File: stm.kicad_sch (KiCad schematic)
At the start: 0 parts

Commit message: added some components
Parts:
- added C? (x4): 100n, symbol Device:C
- added C?: 10n, symbol Device:C
- added C? (x2): 1u, symbol Device:C
- added C?: 10u, symbol Device:C
- added FB?: FerriteBead, symbol Device:FerriteBead
- added U?: STM32F103C8Tx, Package_QFP:LQFP-48_7x7mm_P0.5mm, symbol MCU_ST_STM32F1:STM32F103C8Tx
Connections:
- new net: C?.1, FB?.2
- new net +3.3V: C?.1, C?.1, C?.1, C?.1, C?.1, C?.1, C?.1, FB?.1, U?.1 (VBAT), U?.24 (VDD), U?.36 (VDD), U?.48 (VDD), U?.9 (VDDA)
- new net GND: C?.2, C?.2, C?.2, C?.2, C?.2, C?.2, C?.2, C?.2, U?.23 (VSS), U?.35 (VSS), U?.47 (VSS), U?.8 (VSSA)

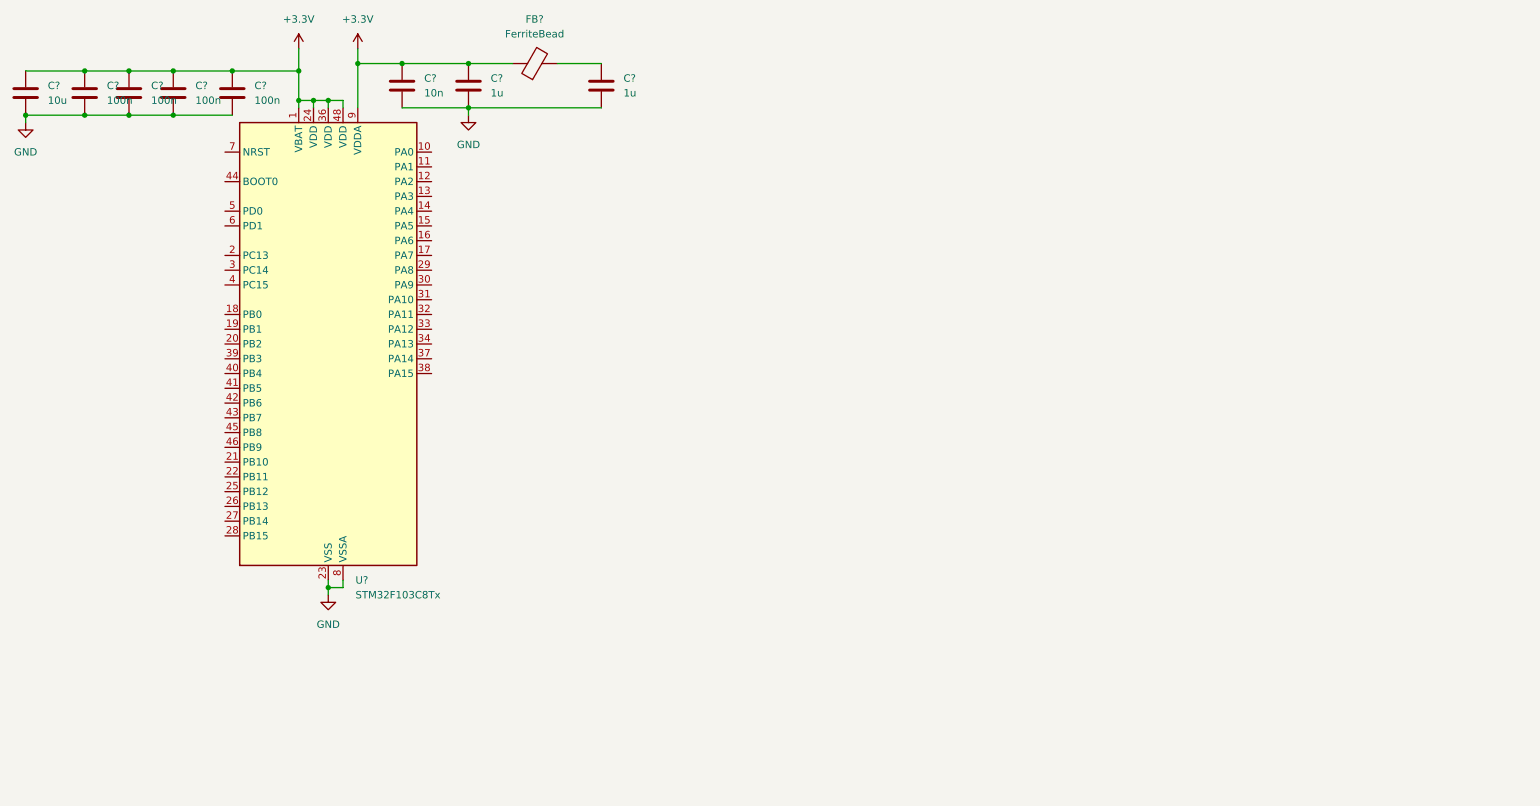
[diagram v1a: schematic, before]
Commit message: added more to schematic
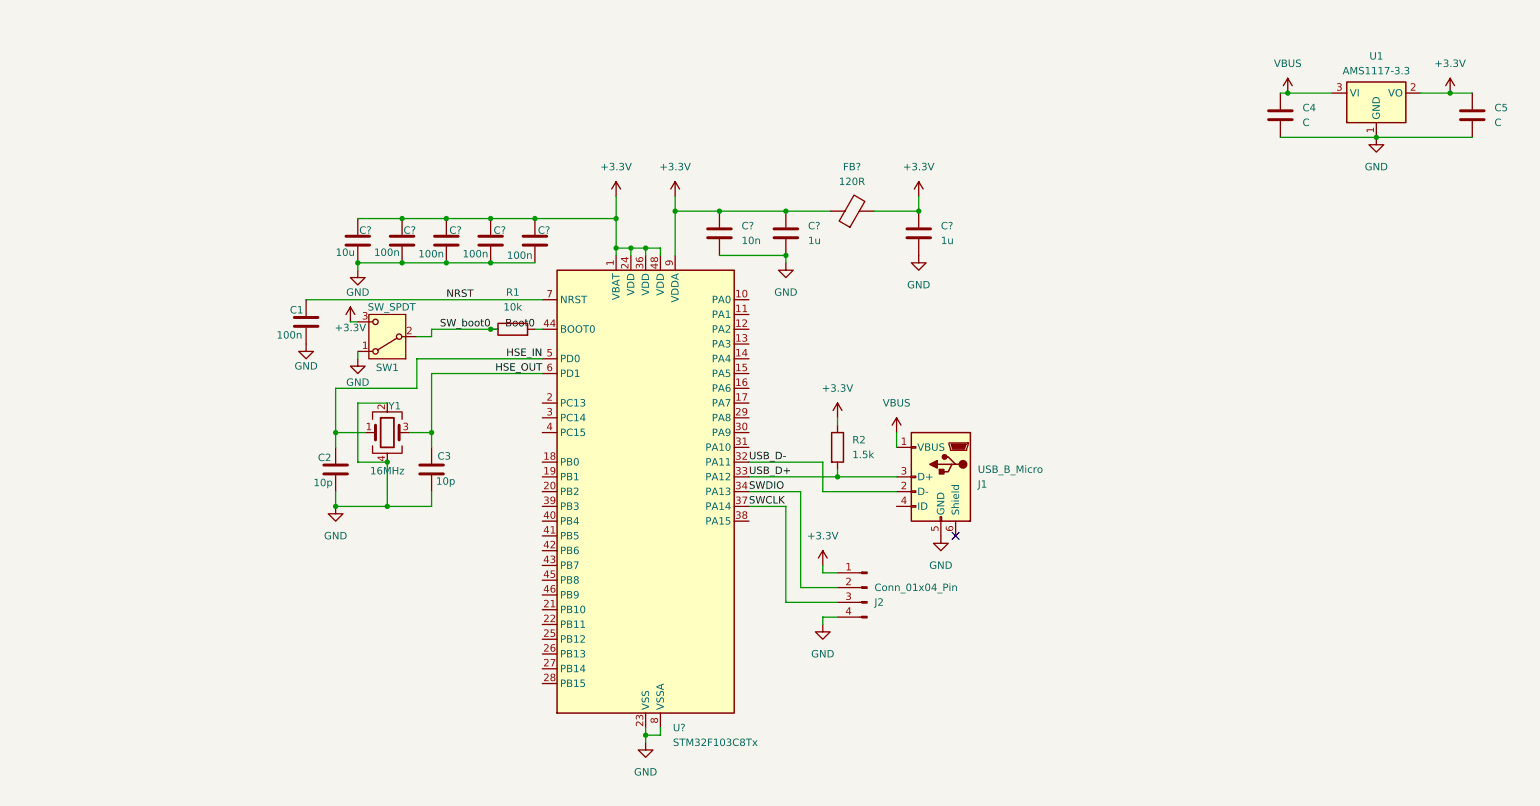
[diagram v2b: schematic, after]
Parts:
- added C1: 100n, symbol Device:C
- added C2, C3: 10p, symbol Device:C
- added C4, C5: C, symbol Device:C
- added J1: USB_B_Micro, symbol Connector:USB_B_Micro
- added J2: Conn_01x04_Pin, symbol Connector:Conn_01x04_Pin
- added R1: 10k, symbol Device:R
- added R2: 1.5k, symbol Device:R
- added SW1: SW_SPDT, symbol Switch:SW_SPDT
- added U1: AMS1117-3.3, Package_TO_SOT_SMD:SOT-223-3_TabPin2, symbol Regulator_Linear:AMS1117-3.3
- added Y1: 16MHz, symbol Device:Crystal_GND24
- FB?: value FerriteBead -> 120R
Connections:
- net +3.3V: now also C?.1, FB?.2, C5.1, J2.1 (Pin_1), R2.1, SW1.3 (C), U1.2 (VO)
- net GND: now also C1.1, C2.2, C3.2, C4.2, C5.2, J1.5 (GND), J2.4 (Pin_4), SW1.1 (A), U1.1 (GND), Y1.2, Y1.4
- net USB_D-: now reaches U?.32 (PA11)
- net USB_D-: now also J1.2 (D-)
- net USB_D+: now reaches U?.33 (PA12)
- net USB_D+: now also J1.3 (D+), R2.2
- net SWDIO: now reaches U?.34 (PA13)
- net SWDIO: now also J2.2 (Pin_2)
- net SWCLK: now reaches U?.37 (PA14)
- net SWCLK: now also J2.3 (Pin_3)
- net Boot0: now reaches U?.44 (BOOT0)
- net Boot0: now also R1.2
- net HSE_IN: now reaches U?.5 (PD0)
- net HSE_IN: now also C2.1, Y1.1
- net HSE_OUT: now reaches U?.6 (PD1)
- net HSE_OUT: now also C3.1, Y1.3
- net NRST: now reaches U?.7 (NRST)
- net NRST: now also C1.2
- new net SW_boot0: R1.1, SW1.2 (B)
- new net VBUS: C4.1, J1.1 (VBUS), U1.3 (VI)
- no-connect marks 0 -> 1
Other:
- moved on the sheet: C?, FB?, U?

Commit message: done with schematic
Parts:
- added D1: LED, LED_SMD:LED_0805_2012Metric_Pad1.15x1.40mm_HandSolder, symbol Device:LED
- added J3, J4: Conn_01x04_Pin, Connector_PinHeader_2.54mm:PinHeader_1x04_P2.54mm_Vertical, symbol Connector:Conn_01x04_Pin
- added R3, R4, R5: 1.5k, Resistor_SMD:R_0402_1005Metric_Pad0.72x0.64mm_HandSolder, symbol Device:R
- C1, C2, C3: footprint (none) -> Capacitor_SMD:C_0805_2012Metric_Pad1.18x1.45mm_HandSolder
- C10, C11, C12, C13, C6, C7, C8, C9: renamed from C?; footprint (none) -> Capacitor_SMD:C_0805_2012Metric_Pad1.18x1.45mm_HandSolder
- C4, C5: value C -> 22u; footprint (none) -> Capacitor_SMD:C_0805_2012Metric_Pad1.18x1.45mm_HandSolder
- FB1: renamed from FB?; footprint (none) -> Inductor_SMD:L_0603_1608Metric_Pad1.05x0.95mm_HandSolder
- J1: footprint (none) -> Connector_USB:USB_Micro-B_Molex_47346-0001
- J2: footprint (none) -> Connector_PinHeader_2.54mm:PinHeader_1x04_P2.54mm_Vertical
- R1, R2: footprint (none) -> Resistor_SMD:R_0402_1005Metric_Pad0.72x0.64mm_HandSolder
- SW1: footprint (none) -> Button_Switch_SMD:SW_SPST_B3S-1100
- Y1: footprint (none) -> Crystal:Crystal_SMD_3225-4Pin_3.2x2.5mm_HandSoldering
- gave numbers to parts that had none: 1
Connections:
- net +3.3V: now also D1.2 (A), J3.1 (Pin_1), J4.1 (Pin_1), R4.1, R5.1
- net GND: now also J3.4 (Pin_4), J4.4 (Pin_4), R3.2
- net I2C2_SCL: now reaches U2.21 (PB10)
- net I2C2_SCL: now also J4.2 (Pin_2), R4.2
- net I2C2_SDA: now reaches U2.22 (PB11)
- net I2C2_SDA: now also J4.3 (Pin_3), R5.2
- net UART_TX: now reaches U2.42 (PB6)
- net UART_TX: now also J3.2 (Pin_2)
- net UART_RX: now reaches U2.43 (PB7)
- net UART_RX: now also J3.3 (Pin_3)
- new net PWR_LED_Cathode: D1.1 (K), R3.1
- no-connect marks 1 -> 28
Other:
- note added: "1x 100nF cap per VDD or VBAT pin"
- note added: "Microcontroller and Micro USB"
- note added: "Pin-out done using STM32CubeIDE software"
- note added: "Power Supply"
- note added: "VBUS from USB con (typ +5V). 22u min in/out cap."
- note added: "application note AN4879 - 2.1: USB implementation on STM32 products"
- note added: "extra filtering for VDDA"
- company: (none) -> I love KiCAD inc.
- title: (none) -> STM32 Microcontroller
- moved on the sheet: C4, C5, U1

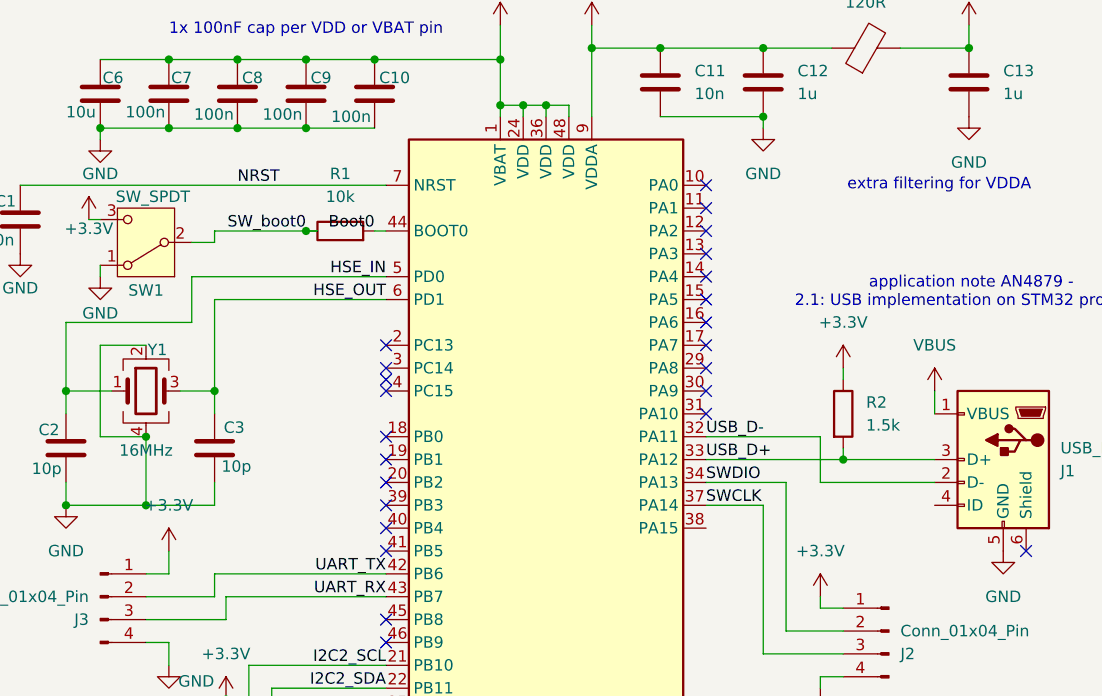
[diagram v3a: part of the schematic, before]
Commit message: fixed all DRC errors
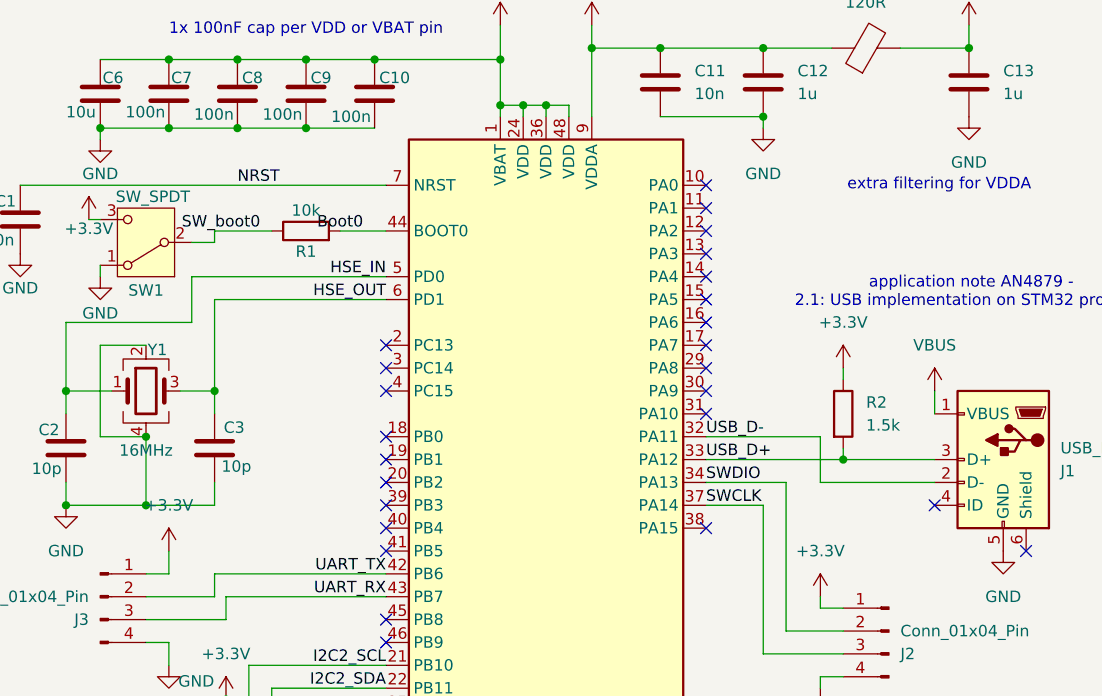
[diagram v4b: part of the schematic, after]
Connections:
- no-connect marks 28 -> 29
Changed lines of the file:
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@@
 	)
 	(junction
-		(at 105.41 69.85)
-		(diameter 0)
-		(color 0 0 0 0)
-	)
-	(junction
 		(at 165.1 95.25)
 		(diameter 0)
@@
 	)
 	(no_connect
-		(at 114.3 130.81)
+		(at 149.86 102.87)
 	)
 	(no_connect
-		(at 114.3 86.36)
+		(at 114.3 130.81)
 	)
 	(no_connect
@@
 	)
 	(no_connect
-		(at 114.3 87.63)
-	)
-	(no_connect
 		(at 114.3 102.87)
 	)
@@
 	)
 	(no_connect
+		(at 175.26 100.33)
+	)
+	(no_connect
+		(at 114.3 87.63)
+	)
+	(no_connect
 		(at 149.86 85.09)
 	)
@@
 	(wire
 		(pts
-			(xy 105.41 58.42) (xy 113.03 58.42)
+			(xy 95.25 69.85) (xy 101.6 69.85)
 		)
 		(stroke
@@
 	(wire
 		(pts
-			(xy 134.62 139.7) (xy 132.08 139.7)
+			(xy 105.41 58.42) (xy 113.03 58.42)
 		)
 		(stroke
@@
 	(wire
 		(pts
-			(xy 78.74 87.63) (xy 83.82 87.63)
+			(xy 134.62 139.7) (xy 132.08 139.7)
 		)
 		(stroke
@@
 	(wire
 		(pts
-			(xy 87.63 113.03) (xy 96.52 113.03)
+			(xy 78.74 87.63) (xy 83.82 87.63)
 		)
 		(stroke
@@
 	(wire
 		(pts
-			(xy 223.52 29.21) (xy 231.14 29.21)
+			(xy 87.63 113.03) (xy 96.52 113.03)
 		)
 		(stroke
@@
 	(wire
 		(pts
-			(xy 95.25 97.79) (xy 95.25 100.33)
+			(xy 223.52 29.21) (xy 231.14 29.21)
 		)
 		(stroke
@@
 	(wire
 		(pts
-			(xy 156.21 100.33) (xy 149.86 100.33)
+			(xy 95.25 97.79) (xy 95.25 100.33)
 		)
 		(stroke
@@
 	(wire
 		(pts
-			(xy 95.25 87.63) (xy 95.25 77.47)
+			(xy 156.21 100.33) (xy 149.86 100.33)
 		)
 		(stroke
@@
 	(wire
 		(pts
-			(xy 106.68 69.85) (xy 105.41 69.85)
+			(xy 95.25 87.63) (xy 95.25 77.47)
 		)
 		(stroke
@@
 	(wire
 		(pts
-			(xy 95.25 69.85) (xy 105.41 69.85)
-		)
-		(stroke
-			(width 0)
-			(type default)
-		)
-	)
-	(wire
-		(pts
 			(xy 162.56 97.79) (xy 162.56 92.71)
 		)
@@
 	(wire
 		(pts
-			(xy 113.03 69.85) (xy 114.3 69.85)
-		)
-		(stroke
-			(width 0)
-			(type default)
-		)
-	)
-	(wire
-		(pts
 			(xy 92.71 71.12) (xy 95.25 71.12)
 		)
@@
 	(wire
 		(pts
+			(xy 109.22 69.85) (xy 114.3 69.85)
+		)
+		(stroke
+			(width 0)
+			(type default)
+		)
+	)
+	(wire
+		(pts
 			(xy 156.21 58.42) (xy 156.21 57.15)
 		)
@@
 	)
 	(label "Boot0"
-		(at 113.03 69.85 180)
+		(at 111.76 69.85 180)
 		(effects
 			(font
@@
 	)
 	(label "SW_boot0"
-		(at 105.41 69.85 180)
+		(at 100.33 69.85 180)
 		(effects
 			(font
@@
 	)
 	(symbol
-		(lib_id "power:GND")
-		(at 179.07 57.15 0)
+		(lib_id "Device:R")
+		(at 105.41 69.85 90)
 		(unit 1)
 		(exclude_from_sim no)
@@
 		(on_board yes)
 		(dnp no)
-		(fields_autoplaced yes)
-		(property "Reference" "#PWR06"
-			(at 179.07 63.5 0)
+		(property "Reference" "R1"
+			(at 105.41 72.136 90)
 			(effects
 				(font
 					(size 1.27 1.27)
 				)
-				(hide yes)
 			)
 		)
-		(property "Value" "GND"
-			(at 179.07 62.23 0)
+		(property "Value" "10k"
+			(at 105.41 67.564 90)
 			(effects
 				(font
@@
 			)
 		)
-		(property "Footprint" ""
-			(at 179.07 57.15 0)
+		(property "Footprint" "Resistor_SMD:R_0402_1005Metric_Pad0.72x0.64mm_HandSolder"
+			(at 105.41 71.628 90)
 			(effects
 				(font
@@
 			)
 		)
-		(property "Datasheet" ""
-			(at 179.07 57.15 0)
+		(property "Datasheet" "~"
+			(at 105.41 69.85 0)
 			(effects
 				(font
@@
 			)
 		)
-		(property "Description" "Power symbol creates a global label with name \"GND\" , ground"
-			(at 179.07 57.15 0)
+		(property "Description" "Resistor"
+			(at 105.41 69.85 0)
 			(effects
 				(font
@@
 			)
 		)
+		(pin "2"
+		)
 		(pin "1"
 		)
 		(instances
-			(project "stm"
+			(project ""
 				(path "/ec652fd4-c034-4510-acc4-5860b93bab77"
-					(reference "#PWR06")
+					(reference "R1")
 					(unit 1)
 				)
@@
 	)
 	(symbol
-		(lib_id "Device:R")
-		(at 109.22 69.85 90)
+		(lib_id "power:GND")
+		(at 179.07 57.15 0)
 		(unit 1)
 		(exclude_from_sim no)
@@
 		(dnp no)
 		(fields_autoplaced yes)
-		(property "Reference" "R1"
-			(at 109.22 63.5 90)
+		(property "Reference" "#PWR06"
+			(at 179.07 63.5 0)
 			(effects
 				(font
 					(size 1.27 1.27)
 				)
+				(hide yes)
 			)
 		)
-		(property "Value" "10k"
-			(at 109.22 66.04 90)
+		(property "Value" "GND"
+			(at 179.07 62.23 0)
 			(effects
 				(font
@@
 			)
 		)
-		(property "Footprint" "Resistor_SMD:R_0402_1005Metric_Pad0.72x0.64mm_HandSolder"
-			(at 109.22 71.628 90)
+		(property "Footprint" ""
+			(at 179.07 57.15 0)
 			(effects
 				(font
@@
 			)
 		)
-		(property "Datasheet" "~"
-			(at 109.22 69.85 0)
+		(property "Datasheet" ""
+			(at 179.07 57.15 0)
 			(effects
 				(font
@@
 			)
 		)
-		(property "Description" "Resistor"
-			(at 109.22 69.85 0)
+		(property "Description" "Power symbol creates a global label with name \"GND\" , ground"
+			(at 179.07 57.15 0)
 			(effects
 				(font
@@
 			)
 		)
-		(pin "2"
-		)
 		(pin "1"
 		)
 		(instances
-			(project ""
+			(project "stm"
 				(path "/ec652fd4-c034-4510-acc4-5860b93bab77"
-					(reference "R1")
+					(reference "#PWR06")
 					(unit 1)
 				)

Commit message: started design of layout
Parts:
- C1, C10, C11, C12, C13, C2, C3, C7, C8, C9: footprint Capacitor_SMD:C_0805_2012Metric_Pad1.18x1.45mm_HandSolder -> Capacitor_SMD:C_0402_1005Metric_Pad0.74x0.62mm_HandSolder
- C6: footprint Capacitor_SMD:C_0805_2012Metric_Pad1.18x1.45mm_HandSolder -> Capacitor_SMD:C_0603_1608Metric_Pad1.08x0.95mm_HandSolder
- SW1: footprint Button_Switch_SMD:SW_SPST_B3S-1100 -> Button_Switch_SMD:Nidec_Copal_CAS-120A
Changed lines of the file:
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@@
 			)
 		)
-		(property "Footprint" "Capacitor_SMD:C_0805_2012Metric_Pad1.18x1.45mm_HandSolder"
+		(property "Footprint" "Capacitor_SMD:C_0402_1005Metric_Pad0.74x0.62mm_HandSolder"
 			(at 98.7552 58.42 0)
 			(effects
@@
 			)
 		)
-		(property "Footprint" "Button_Switch_SMD:SW_SPST_B3S-1100"
+		(property "Footprint" "Button_Switch_SMD:Nidec_Copal_CAS-120A"
 			(at 87.63 71.12 0)
 			(effects
@@
 			)
 		)
-		(property "Footprint" "Capacitor_SMD:C_0805_2012Metric_Pad1.18x1.45mm_HandSolder"
+		(property "Footprint" "Capacitor_SMD:C_0402_1005Metric_Pad0.74x0.62mm_HandSolder"
 			(at 96.2152 97.79 0)
 			(effects
@@
 			)
 		)
-		(property "Footprint" "Capacitor_SMD:C_0805_2012Metric_Pad1.18x1.45mm_HandSolder"
+		(property "Footprint" "Capacitor_SMD:C_0402_1005Metric_Pad0.74x0.62mm_HandSolder"
 			(at 106.3752 58.42 0)
 			(effects
@@
 			)
 		)
-		(property "Footprint" "Capacitor_SMD:C_0805_2012Metric_Pad1.18x1.45mm_HandSolder"
+		(property "Footprint" "Capacitor_SMD:C_0402_1005Metric_Pad0.74x0.62mm_HandSolder"
 			(at 145.7452 57.15 0)
 			(effects
@@
 			)
 		)
-		(property "Footprint" "Capacitor_SMD:C_0805_2012Metric_Pad1.18x1.45mm_HandSolder"
+		(property "Footprint" "Capacitor_SMD:C_0402_1005Metric_Pad0.74x0.62mm_HandSolder"
 			(at 91.1352 58.42 0)
 			(effects
@@
 			)
 		)
-		(property "Footprint" "Capacitor_SMD:C_0805_2012Metric_Pad1.18x1.45mm_HandSolder"
+		(property "Footprint" "Capacitor_SMD:C_0402_1005Metric_Pad0.74x0.62mm_HandSolder"
 			(at 113.9952 58.42 0)
 			(effects
@@
 			)
 		)
-		(property "Footprint" "Capacitor_SMD:C_0805_2012Metric_Pad1.18x1.45mm_HandSolder"
+		(property "Footprint" "Capacitor_SMD:C_0402_1005Metric_Pad0.74x0.62mm_HandSolder"
 			(at 180.0352 57.15 0)
 			(effects
@@
 			)
 		)
-		(property "Footprint" "Capacitor_SMD:C_0805_2012Metric_Pad1.18x1.45mm_HandSolder"
+		(property "Footprint" "Capacitor_SMD:C_0402_1005Metric_Pad0.74x0.62mm_HandSolder"
 			(at 79.7052 97.79 0)
 			(effects
@@
 			)
 		)
-		(property "Footprint" "Capacitor_SMD:C_0805_2012Metric_Pad1.18x1.45mm_HandSolder"
+		(property "Footprint" "Capacitor_SMD:C_0603_1608Metric_Pad1.08x0.95mm_HandSolder"
 			(at 83.5152 58.42 0)
 			(effects
@@
 			)
 		)
-		(property "Footprint" "Capacitor_SMD:C_0805_2012Metric_Pad1.18x1.45mm_HandSolder"
+		(property "Footprint" "Capacitor_SMD:C_0402_1005Metric_Pad0.74x0.62mm_HandSolder"
 			(at 157.1752 57.15 0)
 			(effects
@@
 			)
 		)
-		(property "Footprint" "Capacitor_SMD:C_0805_2012Metric_Pad1.18x1.45mm_HandSolder"
+		(property "Footprint" "Capacitor_SMD:C_0402_1005Metric_Pad0.74x0.62mm_HandSolder"
 			(at 72.6948 64.77 0)
 			(effects

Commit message: changed layout design
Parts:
- added H1, H2, H3, H4: MountingHole, MountingHole:MountingHole_2.1mm, symbol Mechanical:MountingHole
- SW1: footprint Button_Switch_SMD:Nidec_Copal_CAS-120A -> Button_Switch_SMD:SW_SPST_B3U-1100P-B
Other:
- note added: "Mounting holes"

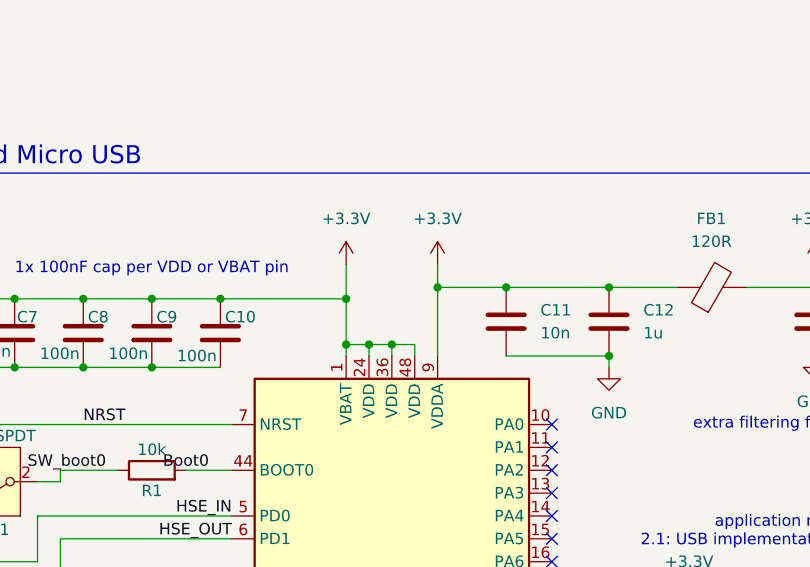
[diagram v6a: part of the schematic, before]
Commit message: added routing, need to change size of pwr routes and connect all GND to gnd plane
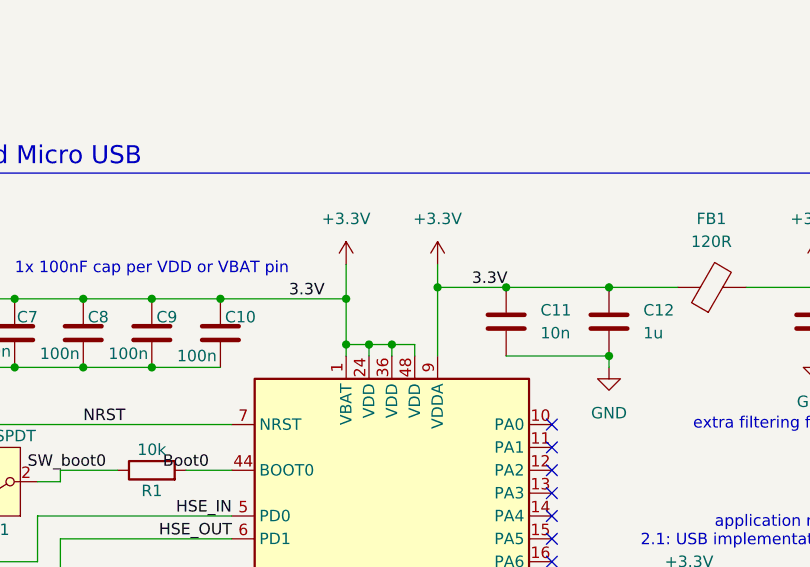
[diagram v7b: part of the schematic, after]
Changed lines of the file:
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@@
+		)
+	)
+	(label "3.3V"
+		(at 140.97 49.53 0)
+		(effects
+			(font
+				(size 1.27 1.27)
+			)
+			(justify left bottom)
 		)
 	)
@@
 		(effects
 			(font
+				(size 1.27 1.27)
+			)
+			(justify left bottom)
+		)
+	)
+	(label "3.3V"
+		(at 120.65 50.8 0)
+		(effects
+			(font
